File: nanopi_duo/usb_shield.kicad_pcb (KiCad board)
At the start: 2 copper layers, 70 x 30 mm, 12 parts, among them J1 USB_A, J2 USB_A, U1 NanoPi Duo

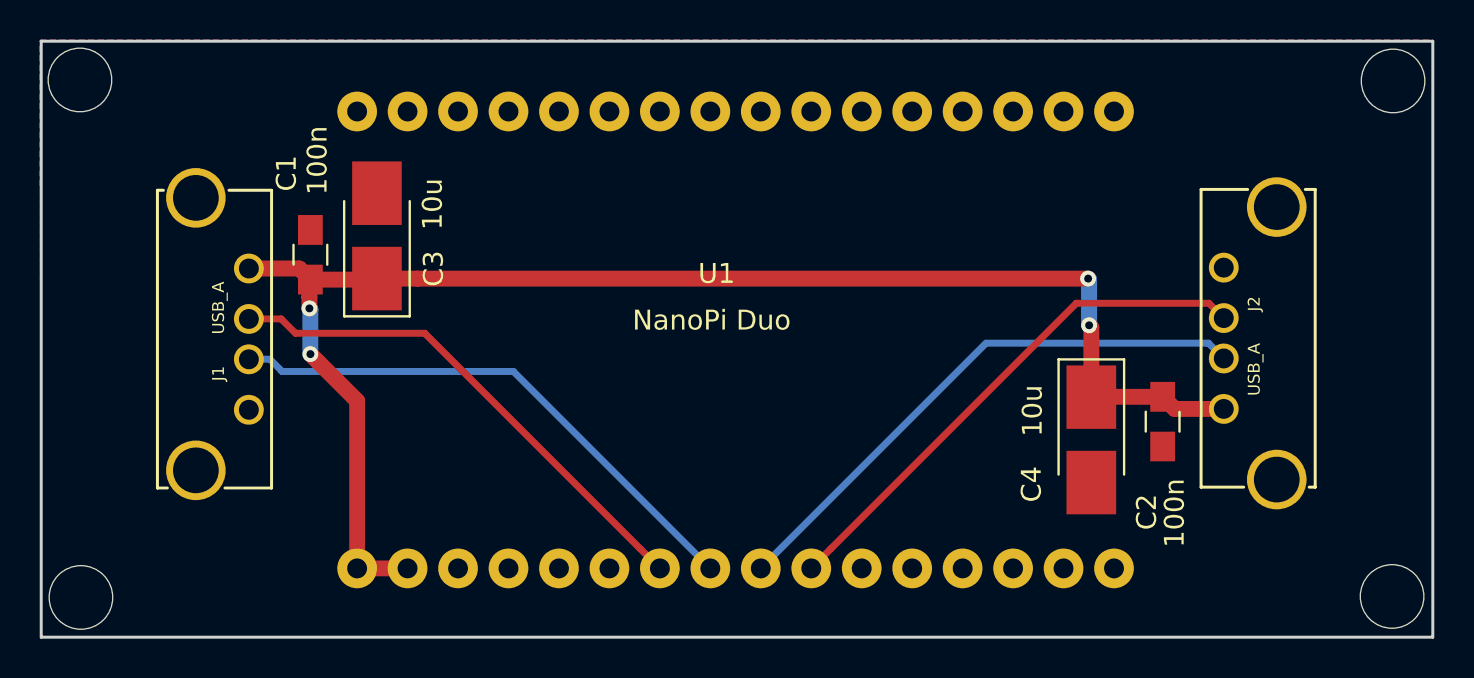
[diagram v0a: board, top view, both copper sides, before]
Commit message: nano pi duo usb shield - stitching vias
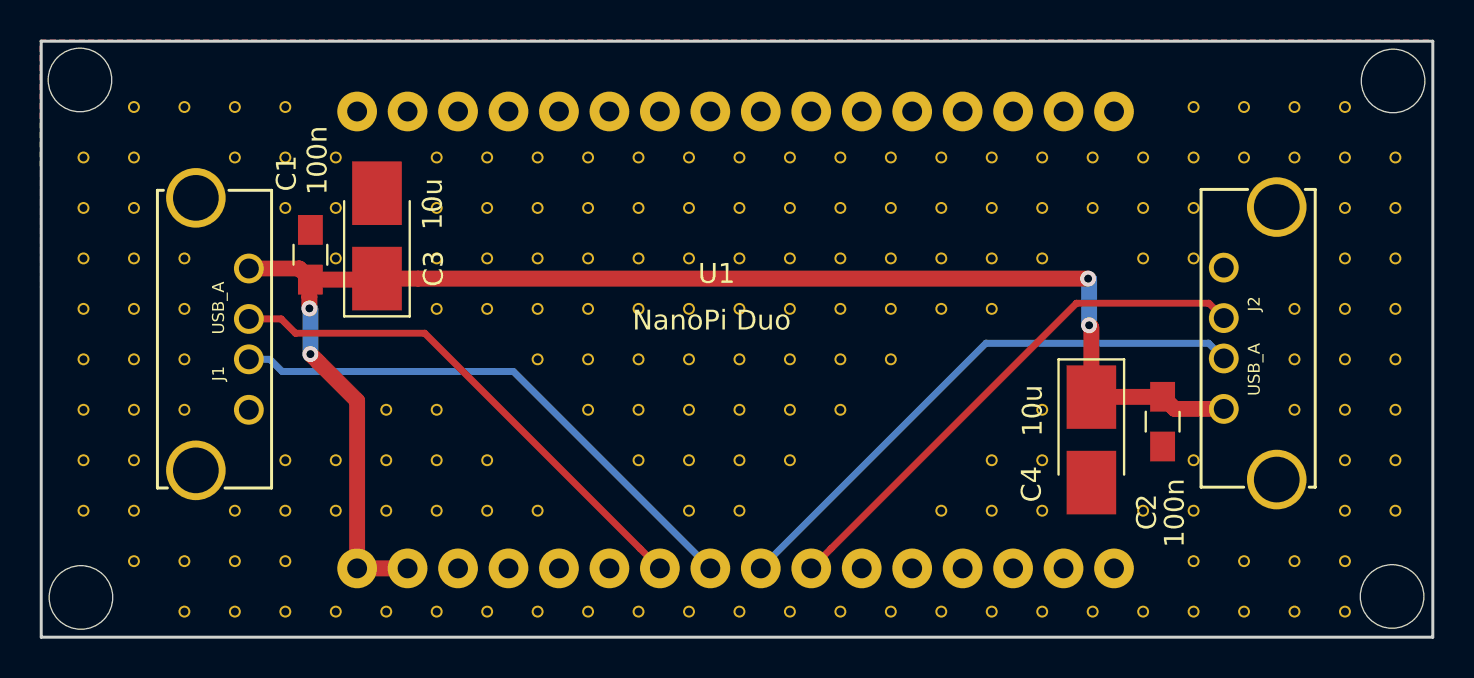
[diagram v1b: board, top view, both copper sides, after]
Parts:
- added V10_10: AUTO_VIA, VIA_MATRIX, F.Cu at (134.2, 112.0)
- added V10_11: AUTO_VIA, VIA_MATRIX, F.Cu at (134.2, 114.5)
- added V10_13: AUTO_VIA, VIA_MATRIX, F.Cu at (134.2, 119.6)
- added V10_9: AUTO_VIA, VIA_MATRIX, F.Cu at (134.2, 109.5)
- added V11_10: AUTO_VIA, VIA_MATRIX, F.Cu at (136.7, 112.0)
- added V11_11: AUTO_VIA, VIA_MATRIX, F.Cu at (136.7, 114.5)
- added V11_13: AUTO_VIA, VIA_MATRIX, F.Cu at (136.7, 119.6)
- added V11_4: AUTO_VIA, VIA_MATRIX, F.Cu at (136.7, 96.8)
- added V11_5: AUTO_VIA, VIA_MATRIX, F.Cu at (136.7, 99.3)
- added V11_6: AUTO_VIA, VIA_MATRIX, F.Cu at (136.7, 101.8)
- added V11_7: AUTO_VIA, VIA_MATRIX, F.Cu at (136.7, 104.4)
- added V11_9: AUTO_VIA, VIA_MATRIX, F.Cu at (136.7, 109.5)
- added V12_10: AUTO_VIA, VIA_MATRIX, F.Cu at (139.2, 112.0)
- added V12_11: AUTO_VIA, VIA_MATRIX, F.Cu at (139.2, 114.5)
- added V12_13: AUTO_VIA, VIA_MATRIX, F.Cu at (139.2, 119.6)
- added V12_4: AUTO_VIA, VIA_MATRIX, F.Cu at (139.2, 96.8)
- added V12_5: AUTO_VIA, VIA_MATRIX, F.Cu at (139.2, 99.3)
- added V12_6: AUTO_VIA, VIA_MATRIX, F.Cu at (139.2, 101.8)
- added V12_7: AUTO_VIA, VIA_MATRIX, F.Cu at (139.2, 104.4)
- added V13_11: AUTO_VIA, VIA_MATRIX, F.Cu at (141.8, 114.5)
- added V13_13: AUTO_VIA, VIA_MATRIX, F.Cu at (141.8, 119.6)
- added V13_4: AUTO_VIA, VIA_MATRIX, F.Cu at (141.8, 96.8)
- added V13_5: AUTO_VIA, VIA_MATRIX, F.Cu at (141.8, 99.3)
- added V13_6: AUTO_VIA, VIA_MATRIX, F.Cu at (141.8, 101.8)
- added V13_7: AUTO_VIA, VIA_MATRIX, F.Cu at (141.8, 104.4)
- added V13_8: AUTO_VIA, VIA_MATRIX, F.Cu at (141.8, 106.9)
- added V14_13: AUTO_VIA, VIA_MATRIX, F.Cu at (144.3, 119.6)
- added V14_4: AUTO_VIA, VIA_MATRIX, F.Cu at (144.3, 96.8)
- added V14_5: AUTO_VIA, VIA_MATRIX, F.Cu at (144.3, 99.3)
- added V14_6: AUTO_VIA, VIA_MATRIX, F.Cu at (144.3, 101.8)
- added V14_7: AUTO_VIA, VIA_MATRIX, F.Cu at (144.3, 104.4)
- added V14_8: AUTO_VIA, VIA_MATRIX, F.Cu at (144.3, 106.9)
- added V14_9: AUTO_VIA, VIA_MATRIX, F.Cu at (144.3, 109.5)
- added V15_10: AUTO_VIA, VIA_MATRIX, F.Cu at (146.9, 112.0)
- added V15_13: AUTO_VIA, VIA_MATRIX, F.Cu at (146.9, 119.6)
- added V15_4: AUTO_VIA, VIA_MATRIX, F.Cu at (146.9, 96.8)
- added V15_5: AUTO_VIA, VIA_MATRIX, F.Cu at (146.9, 99.3)
- added V15_6: AUTO_VIA, VIA_MATRIX, F.Cu at (146.9, 101.8)
- added V15_7: AUTO_VIA, VIA_MATRIX, F.Cu at (146.9, 104.4)
- added V15_8: AUTO_VIA, VIA_MATRIX, F.Cu at (146.9, 106.9)
- added V15_9: AUTO_VIA, VIA_MATRIX, F.Cu at (146.9, 109.5)
- added V16_10: AUTO_VIA, VIA_MATRIX, F.Cu at (149.4, 112.0)
- added V16_11: AUTO_VIA, VIA_MATRIX, F.Cu at (149.4, 114.5)
- added V16_13: AUTO_VIA, VIA_MATRIX, F.Cu at (149.4, 119.6)
- added V16_4: AUTO_VIA, VIA_MATRIX, F.Cu at (149.4, 96.8)
- added V16_5: AUTO_VIA, VIA_MATRIX, F.Cu at (149.4, 99.3)
- added V16_6: AUTO_VIA, VIA_MATRIX, F.Cu at (149.4, 101.8)
- added V16_7: AUTO_VIA, VIA_MATRIX, F.Cu at (149.4, 104.4)
- added V16_8: AUTO_VIA, VIA_MATRIX, F.Cu at (149.4, 106.9)
- added V16_9: AUTO_VIA, VIA_MATRIX, F.Cu at (149.4, 109.5)
- added V17_10: AUTO_VIA, VIA_MATRIX, F.Cu at (151.9, 112.0)
- added V17_11: AUTO_VIA, VIA_MATRIX, F.Cu at (151.9, 114.5)
- added V17_13: AUTO_VIA, VIA_MATRIX, F.Cu at (151.9, 119.6)
- added V17_4: AUTO_VIA, VIA_MATRIX, F.Cu at (151.9, 96.8)
- added V17_5: AUTO_VIA, VIA_MATRIX, F.Cu at (151.9, 99.3)
- added V17_6: AUTO_VIA, VIA_MATRIX, F.Cu at (151.9, 101.8)
- added V17_7: AUTO_VIA, VIA_MATRIX, F.Cu at (151.9, 104.4)
- added V17_8: AUTO_VIA, VIA_MATRIX, F.Cu at (151.9, 106.9)
- added V17_9: AUTO_VIA, VIA_MATRIX, F.Cu at (151.9, 109.5)
- added V18_10: AUTO_VIA, VIA_MATRIX, F.Cu at (154.5, 112.0)
- added V18_13: AUTO_VIA, VIA_MATRIX, F.Cu at (154.5, 119.6)
- added V18_4: AUTO_VIA, VIA_MATRIX, F.Cu at (154.5, 96.8)
- added V18_5: AUTO_VIA, VIA_MATRIX, F.Cu at (154.5, 99.3)
- added V18_6: AUTO_VIA, VIA_MATRIX, F.Cu at (154.5, 101.8)
- added V18_7: AUTO_VIA, VIA_MATRIX, F.Cu at (154.5, 104.4)
- added V18_8: AUTO_VIA, VIA_MATRIX, F.Cu at (154.5, 106.9)
- added V18_9: AUTO_VIA, VIA_MATRIX, F.Cu at (154.5, 109.5)
- added V19_13: AUTO_VIA, VIA_MATRIX, F.Cu at (157.0, 119.6)
- added V19_4: AUTO_VIA, VIA_MATRIX, F.Cu at (157.0, 96.8)
- added V19_5: AUTO_VIA, VIA_MATRIX, F.Cu at (157.0, 99.3)
- added V19_6: AUTO_VIA, VIA_MATRIX, F.Cu at (157.0, 101.8)
- added V19_7: AUTO_VIA, VIA_MATRIX, F.Cu at (157.0, 104.4)
- added V19_8: AUTO_VIA, VIA_MATRIX, F.Cu at (157.0, 106.9)
- added V19_9: AUTO_VIA, VIA_MATRIX, F.Cu at (157.0, 109.5)
- added V20_13: AUTO_VIA, VIA_MATRIX, F.Cu at (159.6, 119.6)
- added V20_4: AUTO_VIA, VIA_MATRIX, F.Cu at (159.6, 96.8)
- added V20_5: AUTO_VIA, VIA_MATRIX, F.Cu at (159.6, 99.3)
- added V20_6: AUTO_VIA, VIA_MATRIX, F.Cu at (159.6, 101.8)
- added V20_7: AUTO_VIA, VIA_MATRIX, F.Cu at (159.6, 104.4)
- added V20_8: AUTO_VIA, VIA_MATRIX, F.Cu at (159.6, 106.9)
- added V21_11: AUTO_VIA, VIA_MATRIX, F.Cu at (162.1, 114.5)
- added V21_13: AUTO_VIA, VIA_MATRIX, F.Cu at (162.1, 119.6)
- added V21_4: AUTO_VIA, VIA_MATRIX, F.Cu at (162.1, 96.8)
- added V21_5: AUTO_VIA, VIA_MATRIX, F.Cu at (162.1, 99.3)
- added V21_6: AUTO_VIA, VIA_MATRIX, F.Cu at (162.1, 101.8)
- added V21_7: AUTO_VIA, VIA_MATRIX, F.Cu at (162.1, 104.4)
- added V22_10: AUTO_VIA, VIA_MATRIX, F.Cu at (164.6, 112.0)
- added V22_11: AUTO_VIA, VIA_MATRIX, F.Cu at (164.6, 114.5)
- added V22_13: AUTO_VIA, VIA_MATRIX, F.Cu at (164.6, 119.6)
- added V22_4: AUTO_VIA, VIA_MATRIX, F.Cu at (164.6, 96.8)
- added V22_5: AUTO_VIA, VIA_MATRIX, F.Cu at (164.6, 99.3)
- added V22_6: AUTO_VIA, VIA_MATRIX, F.Cu at (164.6, 101.8)
- added V22_7: AUTO_VIA, VIA_MATRIX, F.Cu at (164.6, 104.4)
- added V23_10: AUTO_VIA, VIA_MATRIX, F.Cu at (167.2, 112.0)
- added V23_11: AUTO_VIA, VIA_MATRIX, F.Cu at (167.2, 114.5)
- added V23_13: AUTO_VIA, VIA_MATRIX, F.Cu at (167.2, 119.6)
- added V23_4: AUTO_VIA, VIA_MATRIX, F.Cu at (167.2, 96.8)
- added V23_5: AUTO_VIA, VIA_MATRIX, F.Cu at (167.2, 99.3)
- added V23_6: AUTO_VIA, VIA_MATRIX, F.Cu at (167.2, 101.8)
- added V23_9: AUTO_VIA, VIA_MATRIX, F.Cu at (167.2, 109.5)
- added V24_13: AUTO_VIA, VIA_MATRIX, F.Cu at (169.7, 119.6)
- added V24_4: AUTO_VIA, VIA_MATRIX, F.Cu at (169.7, 96.8)
- added V24_5: AUTO_VIA, VIA_MATRIX, F.Cu at (169.7, 99.3)
- added V25_11: AUTO_VIA, VIA_MATRIX, F.Cu at (172.3, 114.5)
- added V25_13: AUTO_VIA, VIA_MATRIX, F.Cu at (172.3, 119.6)
- added V25_4: AUTO_VIA, VIA_MATRIX, F.Cu at (172.3, 96.8)
- added V25_5: AUTO_VIA, VIA_MATRIX, F.Cu at (172.3, 99.3)
- added V25_6: AUTO_VIA, VIA_MATRIX, F.Cu at (172.3, 101.8)
- added V26_10: AUTO_VIA, VIA_MATRIX, F.Cu at (174.8, 112.0)
- added V26_11: AUTO_VIA, VIA_MATRIX, F.Cu at (174.8, 114.5)
- added V26_12: AUTO_VIA, VIA_MATRIX, F.Cu at (174.8, 117.1)
- added V26_13: AUTO_VIA, VIA_MATRIX, F.Cu at (174.8, 119.6)
- added V26_3: AUTO_VIA, VIA_MATRIX, F.Cu at (174.8, 94.2)
- added V26_4: AUTO_VIA, VIA_MATRIX, F.Cu at (174.8, 96.8)
- added V26_5: AUTO_VIA, VIA_MATRIX, F.Cu at (174.8, 99.3)
- added V26_6: AUTO_VIA, VIA_MATRIX, F.Cu at (174.8, 101.8)
- added V27_12: AUTO_VIA, VIA_MATRIX, F.Cu at (177.3, 117.1)
- added V27_13: AUTO_VIA, VIA_MATRIX, F.Cu at (177.3, 119.6)
- added V27_3: AUTO_VIA, VIA_MATRIX, F.Cu at (177.3, 94.2)
- added V27_4: AUTO_VIA, VIA_MATRIX, F.Cu at (177.3, 96.8)
- added V28_12: AUTO_VIA, VIA_MATRIX, F.Cu at (179.9, 117.1)
- added V28_13: AUTO_VIA, VIA_MATRIX, F.Cu at (179.9, 119.6)
- added V28_3: AUTO_VIA, VIA_MATRIX, F.Cu at (179.9, 94.2)
- added V28_4: AUTO_VIA, VIA_MATRIX, F.Cu at (179.9, 96.8)
- added V28_7: AUTO_VIA, VIA_MATRIX, F.Cu at (179.9, 104.4)
- added V28_8: AUTO_VIA, VIA_MATRIX, F.Cu at (179.9, 106.9)
- added V28_9: AUTO_VIA, VIA_MATRIX, F.Cu at (179.9, 109.5)
- added V29_10: AUTO_VIA, VIA_MATRIX, F.Cu at (182.4, 112.0)
- added V29_11: AUTO_VIA, VIA_MATRIX, F.Cu at (182.4, 114.5)
- added V29_12: AUTO_VIA, VIA_MATRIX, F.Cu at (182.4, 117.1)
- added V29_13: AUTO_VIA, VIA_MATRIX, F.Cu at (182.4, 119.6)
- added V29_3: AUTO_VIA, VIA_MATRIX, F.Cu at (182.4, 94.2)
- added V29_4: AUTO_VIA, VIA_MATRIX, F.Cu at (182.4, 96.8)
- added V29_5: AUTO_VIA, VIA_MATRIX, F.Cu at (182.4, 99.3)
- added V29_6: AUTO_VIA, VIA_MATRIX, F.Cu at (182.4, 101.8)
- added V29_7: AUTO_VIA, VIA_MATRIX, F.Cu at (182.4, 104.4)
- added V29_8: AUTO_VIA, VIA_MATRIX, F.Cu at (182.4, 106.9)
- added V29_9: AUTO_VIA, VIA_MATRIX, F.Cu at (182.4, 109.5)
- added V30_10: AUTO_VIA, VIA_MATRIX, F.Cu at (185.0, 112.0)
- added V30_11: AUTO_VIA, VIA_MATRIX, F.Cu at (185.0, 114.5)
- added V30_4: AUTO_VIA, VIA_MATRIX, F.Cu at (185.0, 96.8)
- added V30_5: AUTO_VIA, VIA_MATRIX, F.Cu at (185.0, 99.3)
- added V30_6: AUTO_VIA, VIA_MATRIX, F.Cu at (185.0, 101.8)
- added V30_7: AUTO_VIA, VIA_MATRIX, F.Cu at (185.0, 104.4)
- added V30_8: AUTO_VIA, VIA_MATRIX, F.Cu at (185.0, 106.9)
- added V30_9: AUTO_VIA, VIA_MATRIX, F.Cu at (185.0, 109.5)
- added V4_10: AUTO_VIA, VIA_MATRIX, F.Cu at (118.9, 112.0)
- added V4_11: AUTO_VIA, VIA_MATRIX, F.Cu at (118.9, 114.5)
- added V4_4: AUTO_VIA, VIA_MATRIX, F.Cu at (118.9, 96.8)
- added V4_5: AUTO_VIA, VIA_MATRIX, F.Cu at (118.9, 99.3)
- added V4_6: AUTO_VIA, VIA_MATRIX, F.Cu at (118.9, 101.8)
- added V4_7: AUTO_VIA, VIA_MATRIX, F.Cu at (118.9, 104.4)
- added V4_8: AUTO_VIA, VIA_MATRIX, F.Cu at (118.9, 106.9)
- added V4_9: AUTO_VIA, VIA_MATRIX, F.Cu at (118.9, 109.5)
- added V5_10: AUTO_VIA, VIA_MATRIX, F.Cu at (121.5, 112.0)
- added V5_11: AUTO_VIA, VIA_MATRIX, F.Cu at (121.5, 114.5)
- added V5_12: AUTO_VIA, VIA_MATRIX, F.Cu at (121.5, 117.1)
- added V5_3: AUTO_VIA, VIA_MATRIX, F.Cu at (121.5, 94.2)
- added V5_4: AUTO_VIA, VIA_MATRIX, F.Cu at (121.5, 96.8)
- added V5_5: AUTO_VIA, VIA_MATRIX, F.Cu at (121.5, 99.3)
- added V5_6: AUTO_VIA, VIA_MATRIX, F.Cu at (121.5, 101.8)
- added V5_7: AUTO_VIA, VIA_MATRIX, F.Cu at (121.5, 104.4)
- added V5_8: AUTO_VIA, VIA_MATRIX, F.Cu at (121.5, 106.9)
- added V5_9: AUTO_VIA, VIA_MATRIX, F.Cu at (121.5, 109.5)
- added V6_12: AUTO_VIA, VIA_MATRIX, F.Cu at (124.0, 117.1)
- added V6_13: AUTO_VIA, VIA_MATRIX, F.Cu at (124.0, 119.6)
- added V6_3: AUTO_VIA, VIA_MATRIX, F.Cu at (124.0, 94.2)
- added V6_6: AUTO_VIA, VIA_MATRIX, F.Cu at (124.0, 101.8)
- added V6_7: AUTO_VIA, VIA_MATRIX, F.Cu at (124.0, 104.4)
- added V6_8: AUTO_VIA, VIA_MATRIX, F.Cu at (124.0, 106.9)
- added V6_9: AUTO_VIA, VIA_MATRIX, F.Cu at (124.0, 109.5)
- added V7_11: AUTO_VIA, VIA_MATRIX, F.Cu at (126.5, 114.5)
- added V7_12: AUTO_VIA, VIA_MATRIX, F.Cu at (126.5, 117.1)
- added V7_13: AUTO_VIA, VIA_MATRIX, F.Cu at (126.5, 119.6)
- added V7_3: AUTO_VIA, VIA_MATRIX, F.Cu at (126.5, 94.2)
- added V7_4: AUTO_VIA, VIA_MATRIX, F.Cu at (126.5, 96.8)
- added V8_10: AUTO_VIA, VIA_MATRIX, F.Cu at (129.1, 112.0)
- added V8_11: AUTO_VIA, VIA_MATRIX, F.Cu at (129.1, 114.5)
- added V8_12: AUTO_VIA, VIA_MATRIX, F.Cu at (129.1, 117.1)
- added V8_13: AUTO_VIA, VIA_MATRIX, F.Cu at (129.1, 119.6)
- added V8_3: AUTO_VIA, VIA_MATRIX, F.Cu at (129.1, 94.2)
- added V8_4: AUTO_VIA, VIA_MATRIX, F.Cu at (129.1, 96.8)
- added V8_5: AUTO_VIA, VIA_MATRIX, F.Cu at (129.1, 99.3)
- added V9_10: AUTO_VIA, VIA_MATRIX, F.Cu at (131.6, 112.0)
- added V9_11: AUTO_VIA, VIA_MATRIX, F.Cu at (131.6, 114.5)
- added V9_13: AUTO_VIA, VIA_MATRIX, F.Cu at (131.6, 119.6)
- added V9_4: AUTO_VIA, VIA_MATRIX, F.Cu at (131.6, 96.8)
- added V9_5: AUTO_VIA, VIA_MATRIX, F.Cu at (131.6, 99.3)
- added V9_6: AUTO_VIA, VIA_MATRIX, F.Cu at (131.6, 101.8)
